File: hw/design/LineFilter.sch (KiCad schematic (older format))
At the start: 0 parts

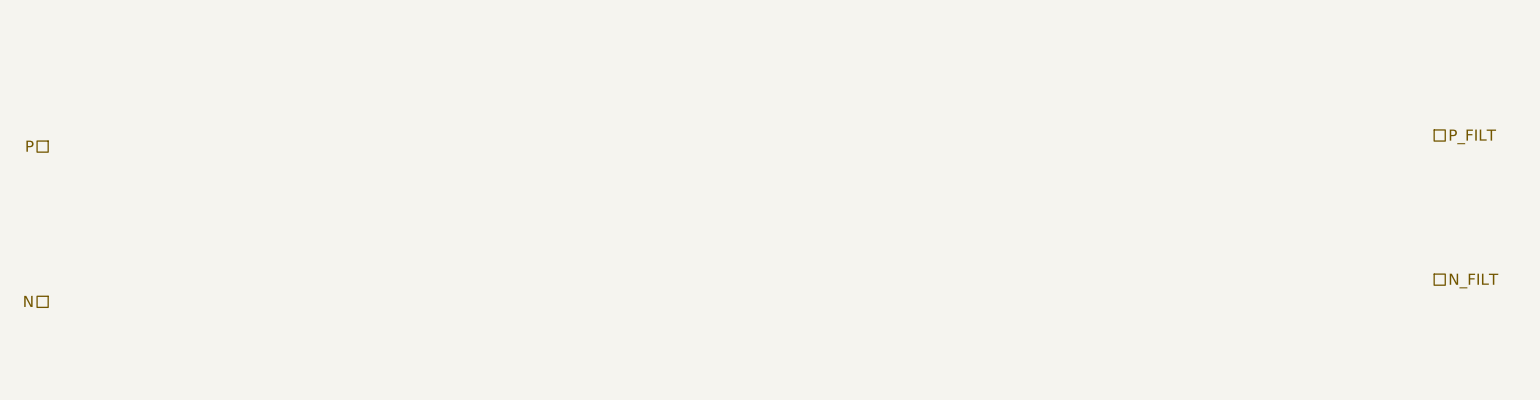
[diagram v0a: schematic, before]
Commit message: aux output, documentation
finished aux output circuit, updated a lot of documentation, added datasheets
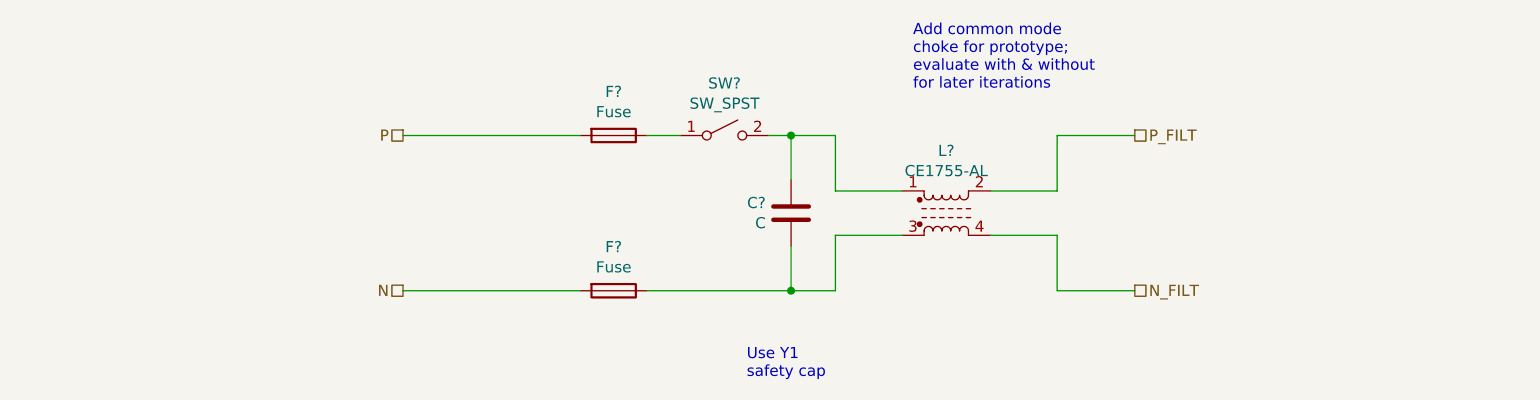
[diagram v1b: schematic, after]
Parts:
- added C?: C, symbol Device:C
- added F? (x2): Fuse, symbol Device:Fuse
- added L?: CE1755-AL, symbol Device:L_Core_Ferrite_Coupled
- added SW?: SW_SPST, symbol Switch:SW_SPST
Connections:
- net N: now also F?.2
- net N_FILT: now also L?.4
- net P: now also F?.2
- net P_FILT: now also L?.2
- new net: F?.1, SW?.1 (A)
- new net: C?.1, F?.1, L?.3
- new net: C?.2, L?.1, SW?.2 (B)
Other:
- note added: "Add common mode\nchoke for prototype;\nevaluate with & without\nfor later iterations"
- note added: "Use Y1\nsafety cap"
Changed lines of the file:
@@
 $Descr A4 11693 8268
 encoding utf-8
-Sheet 8 6
+Sheet 5 7
 Title ""
 Date ""
@@
 Comment4 ""
 $EndDescr
-Text HLabel 1750 2100 0    50   UnSpc ~ 0
+Text HLabel 3350 2050 0    50   UnSpc ~ 0
 P
-Text HLabel 1750 2800 0    50   UnSpc ~ 0
+Text HLabel 3350 2750 0    50   UnSpc ~ 0
 N
-Text HLabel 8000 2050 2    50   UnSpc ~ 0
+Text HLabel 6650 2050 2    50   UnSpc ~ 0
 P_FILT
-Text HLabel 8000 2700 2    50   UnSpc ~ 0
+Text HLabel 6650 2750 2    50   UnSpc ~ 0
 N_FILT
+$Comp
+L Device:Fuse F?
+U 1 1 60433461
+P 4300 2050
+F 0 "F?" V 4103 2050 50  0000 C CNN
+F 1 "Fuse" V 4194 2050 50  0000 C CNN
+F 2 "" V 4230 2050 50  0001 C CNN
+F 3 "~" H 4300 2050 50  0001 C CNN
+	1    4300 2050
+	0    1    1    0
+$EndComp
+$Comp
+L Device:Fuse F?
+U 1 1 6043370A
+P 4300 2750
+F 0 "F?" V 4103 2750 50  0000 C CNN
+F 1 "Fuse" V 4194 2750 50  0000 C CNN
+F 2 "" V 4230 2750 50  0001 C CNN
+F 3 "~" H 4300 2750 50  0001 C CNN
+	1    4300 2750
+	0    1    1    0
+$EndComp
+Wire Wire Line
+	4150 2050 3350 2050
+Wire Wire Line
+	4150 2750 3350 2750
+$Comp
+L Device:C C?
+U 1 1 60433D63
+P 5100 2400
+F 0 "C?" H 4986 2354 50  0000 R CNN
+F 1 "C" H 4986 2445 50  0000 R CNN
+F 2 "" H 5138 2250 50  0001 C CNN
+F 3 "~" H 5100 2400 50  0001 C CNN
+	1    5100 2400
+	1    0    0    1
+$EndComp
+$Comp
+L Switch:SW_SPST SW?
+U 1 1 604348C0
+P 4800 2050
+F 0 "SW?" H 4800 2285 50  0000 C CNN
+F 1 "SW_SPST" H 4800 2194 50  0000 C CNN
+F 2 "" H 4800 2050 50  0001 C CNN
+F 3 "~" H 4800 2050 50  0001 C CNN
+	1    4800 2050
+	1    0    0    -1
+$EndComp
+Wire Wire Line
+	4600 2050 4450 2050
+Wire Wire Line
+	4450 2750 5100 2750
+Wire Wire Line
+	5000 2050 5100 2050
+$Comp
+L Device:L_Core_Ferrite_Coupled L?
+U 1 1 60435934
+P 5800 2400
+F 0 "L?" H 5800 2681 50  0000 C CNN
+F 1 "CE1755-AL" H 5800 2590 50  0000 C CNN
+F 2 "" H 5800 2400 50  0001 C CNN
+F 3 "~" H 5800 2400 50  0001 C CNN
+	1    5800 2400
+	1    0    0    -1
+$EndComp
+Wire Wire Line
+	5300 2050 5300 2300
+Wire Wire Line
+	5300 2300 5600 2300
+Wire Wire Line
+	5600 2500 5300 2500
+Wire Wire Line
+	5300 2500 5300 2750
+Wire Wire Line
+	6000 2300 6300 2300
+Wire Wire Line
+	6300 2300 6300 2050
+Wire Wire Line
+	6300 2050 6650 2050
+Wire Wire Line
+	6000 2500 6300 2500
+Wire Wire Line
+	6300 2500 6300 2750
+Wire Wire Line
+	6300 2750 6650 2750
+Wire Wire Line
+	5100 2250 5100 2050
+Wire Wire Line
+	5100 2550 5100 2750
+Connection ~ 5100 2050
+Wire Wire Line
+	5100 2050 5300 2050
+Connection ~ 5100 2750
+Wire Wire Line
+	5100 2750 5300 2750
+Text Notes 4900 3150 0    50   ~ 0
+Use Y1\nsafety cap
+Text Notes 5650 1850 0    50   ~ 0
+Add common mode\nchoke for prototype;\nevaluate with & without\nfor later iterations
 $EndSCHEMATC

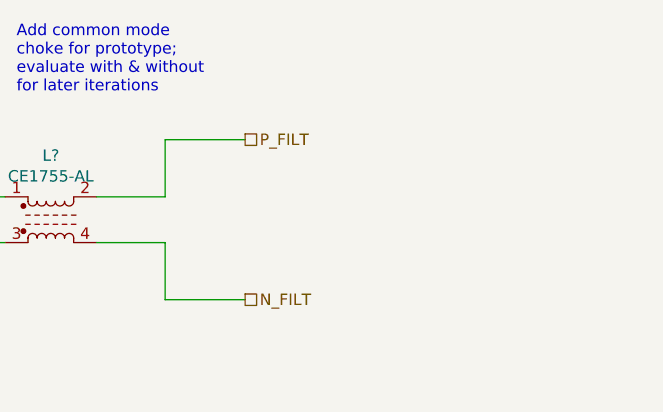
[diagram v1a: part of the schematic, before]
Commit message: label/net reorg, primary SW starting
some reorganization of top-level naming for nets and hierarchical pins

fixed a few part selection issues

started on primary switcher sheet
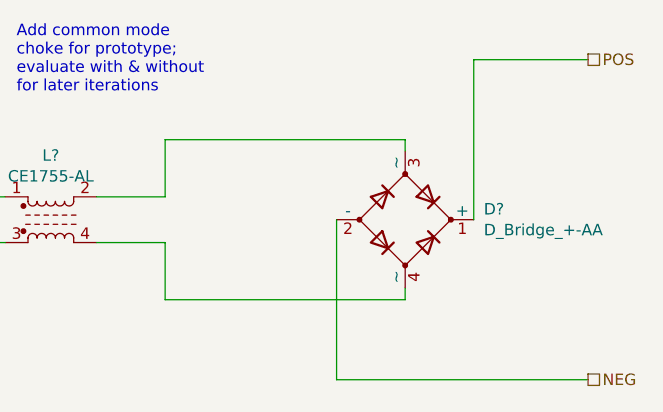
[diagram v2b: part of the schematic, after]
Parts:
- added D?: D_Bridge_+-AA, symbol Device:D_Bridge_+-AA
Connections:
- net N_FILT: no longer names the net of L?.4
- net N_FILT: now also D?.4 (~~)
- net P_FILT: no longer names the net of L?.2
- net P_FILT: now also D?.3 (~~)
- new net NEG: D?.2 (-)
- new net POS: D?.1 (+)
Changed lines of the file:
@@
 $Descr A4 11693 8268
 encoding utf-8
-Sheet 5 7
+Sheet 5 8
 Title ""
 Date ""
@@
 Text HLabel 3350 2750 0    50   UnSpc ~ 0
 N
-Text HLabel 6650 2050 2    50   UnSpc ~ 0
-P_FILT
-Text HLabel 6650 2750 2    50   UnSpc ~ 0
-N_FILT
+Text HLabel 8150 1700 2    50   UnSpc ~ 0
+POS
+Text HLabel 8150 3100 2    50   UnSpc ~ 0
+NEG
 $Comp
 L Device:Fuse F?
@@
 	6300 2300 6300 2050
 Wire Wire Line
-	6300 2050 6650 2050
-Wire Wire Line
 	6000 2500 6300 2500
 Wire Wire Line
 	6300 2500 6300 2750
-Wire Wire Line
-	6300 2750 6650 2750
 Wire Wire Line
 	5100 2250 5100 2050
@@
 Text Notes 5650 1850 0    50   ~ 0
 Add common mode\nchoke for prototype;\nevaluate with & without\nfor later iterations
+$Comp
+L Device:D_Bridge_+-AA D?
+U 1 1 602AF49E
+P 7350 2400
+F 0 "D?" H 7694 2446 50  0000 L CNN
+F 1 "D_Bridge_+-AA" H 7694 2355 50  0000 L CNN
+F 2 "" H 7350 2400 50  0001 C CNN
+F 3 "~" H 7350 2400 50  0001 C CNN
+	1    7350 2400
+	1    0    0    -1
+$EndComp
+Wire Wire Line
+	7650 2400 7650 1700
+Wire Wire Line
+	7650 1700 8150 1700
+Wire Wire Line
+	7050 2400 7050 3100
+Wire Wire Line
+	7050 3100 8150 3100
+Wire Wire Line
+	7350 2750 7350 2700
+Wire Wire Line
+	6300 2750 7350 2750
+Wire Wire Line
+	7350 2050 7350 2100
+Wire Wire Line
+	6300 2050 7350 2050
 $EndSCHEMATC
